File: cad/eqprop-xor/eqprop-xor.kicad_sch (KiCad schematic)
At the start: 31 parts, among them J1 USB_C_Receptacle_USB2.0_14P, U1 MCP6004, U2 LM324

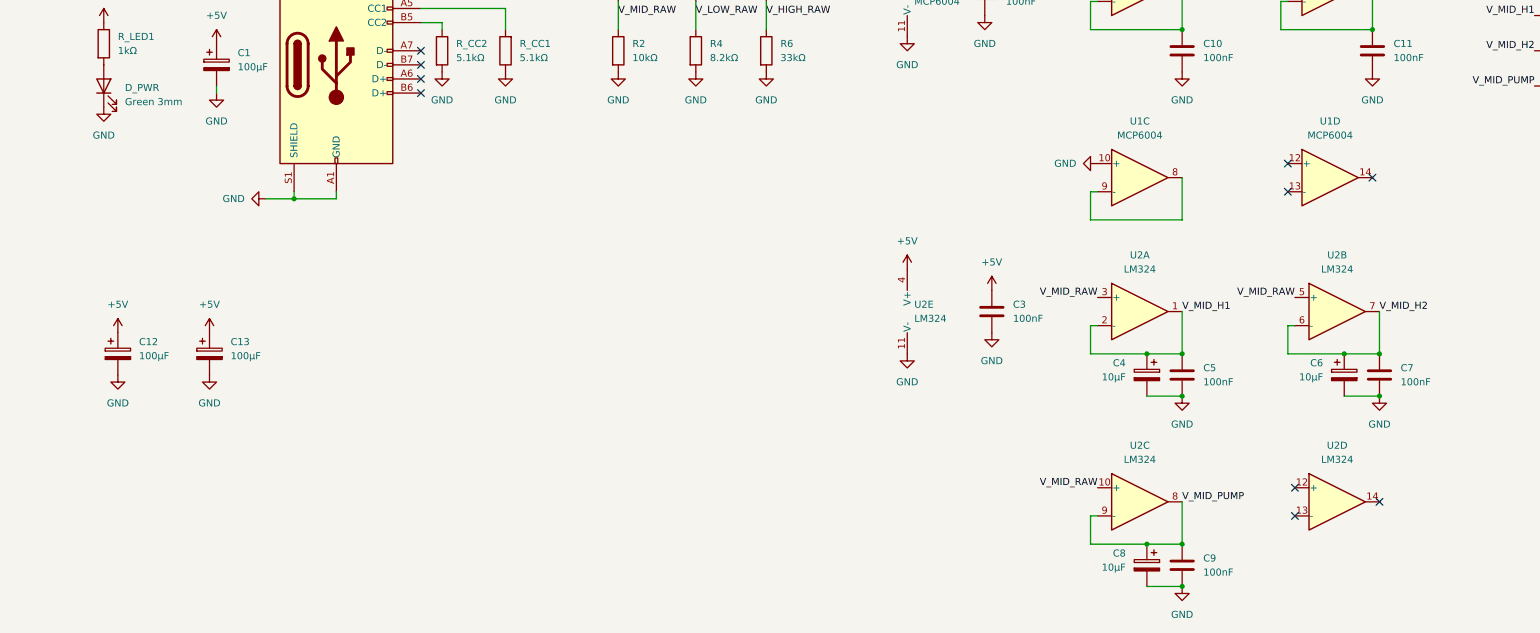
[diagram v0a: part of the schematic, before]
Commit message: Add Arduino Nano section with CS pull-ups and text annotations
Section 2: Arduino Nano pin assignments, 9x 10kΩ CS pull-up resistors,
bulk decoupling caps placed near analog/digital clusters, and text
annotations for readability.

Co-Authored-By: Claude Opus 4.6 <noreply@anthropic.com>
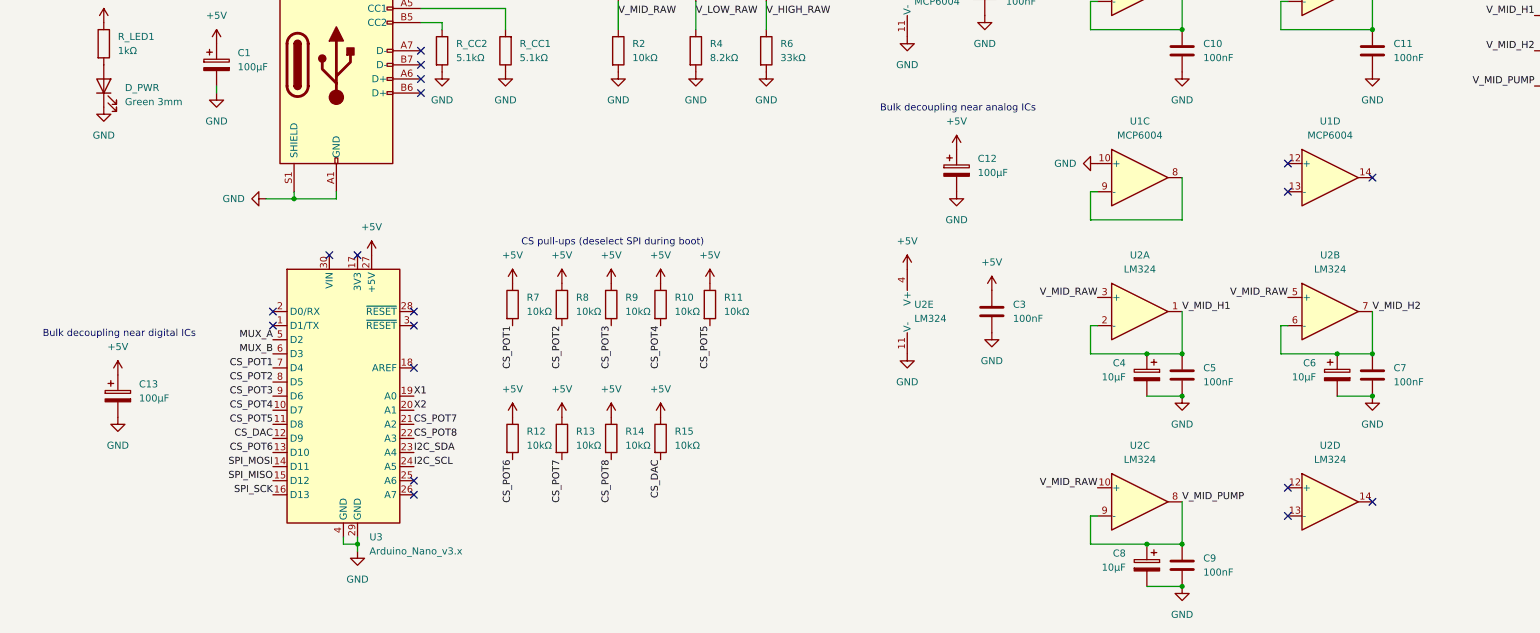
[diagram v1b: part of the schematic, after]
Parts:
- added R10, R11, R12, R13, R14, R15, R7, R8, R9: 10kΩ, symbol Device:R
- added U3: Arduino_Nano_v3.x, Module:Arduino_Nano, symbol MCU_Module:Arduino_Nano_v3.x
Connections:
- net +5V: now also R10.1, R11.1, R12.1, R13.1, R14.1, R15.1, R7.1, R8.1, R9.1, U3.27 (+5V)
- net GND: now also U3.29 (GND), U3.4 (GND)
- new net CS_DAC: R15.2, U3.12 (D9)
- new net CS_POT1: R7.2, U3.7 (D4)
- new net CS_POT2: R8.2, U3.8 (D5)
- new net CS_POT3: R9.2, U3.9 (D6)
- new net CS_POT4: R10.2, U3.10 (D7)
- new net CS_POT5: R11.2, U3.11 (D8)
- new net CS_POT6: R12.2, U3.13 (D10)
- new net CS_POT7: R13.2, U3.21 (A2)
- new net CS_POT8: R14.2, U3.22 (A3)
- new net I2C_SCL: U3.24 (A5)
- new net I2C_SDA: U3.23 (A4)
- new net MUX_A: U3.5 (D2)
- new net MUX_B: U3.6 (D3)
- new net SPI_MISO: U3.15 (D12)
- new net SPI_MOSI: U3.14 (D11)
- new net SPI_SCK: U3.16 (D13)
- new net X1: U3.19 (A0)
- new net X2: U3.20 (A1)
- no-connect marks 10 -> 19
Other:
- note added: "Bulk decoupling near analog ICs"
- note added: "Bulk decoupling near digital ICs"
- note added: "CS pull-ups (deselect SPI during boot)"
- moved on the sheet: C12, C13, C6, C7, U2B, U2D

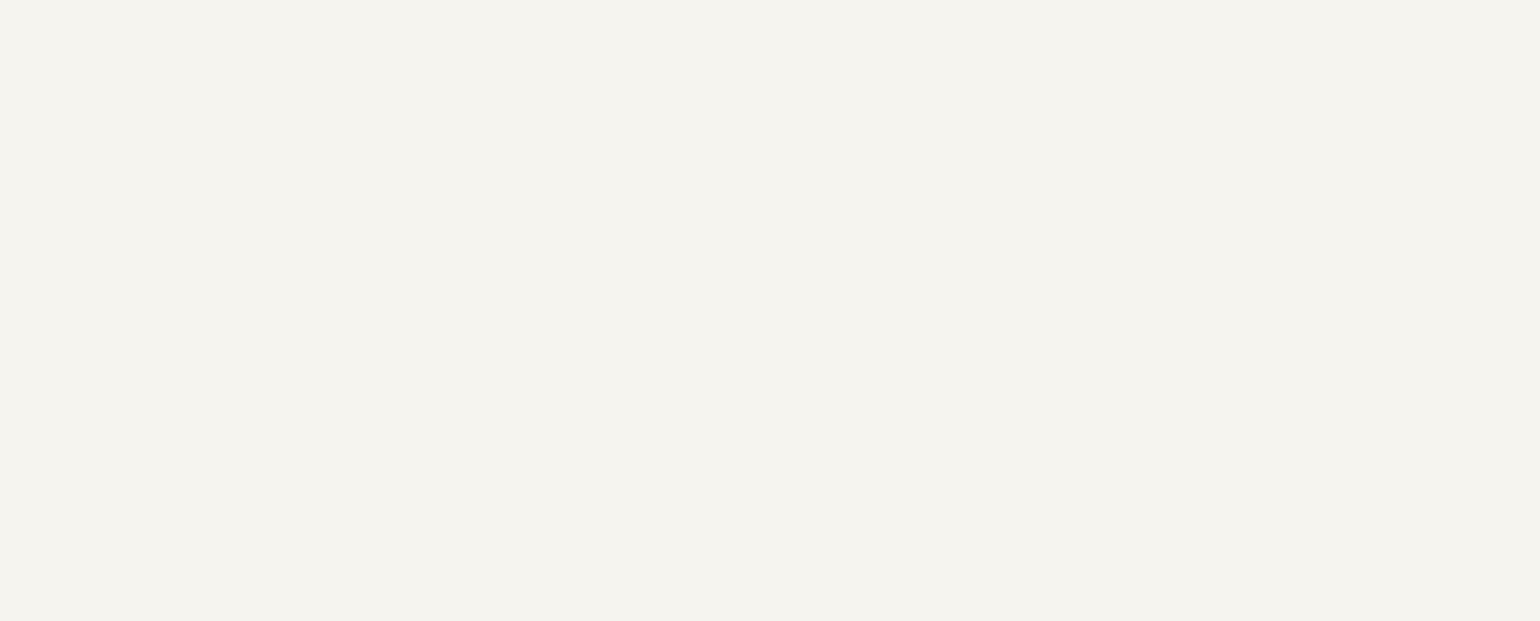
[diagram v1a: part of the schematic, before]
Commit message: Add input muxes and inference toggle switches
Section 3: 2x CD4053B analog muxes (direct + complementary inputs),
decoupling caps, SPDT toggle switches with 10kΩ isolation resistors
for inference mode.

Co-Authored-By: Claude Opus 4.6 <noreply@anthropic.com>
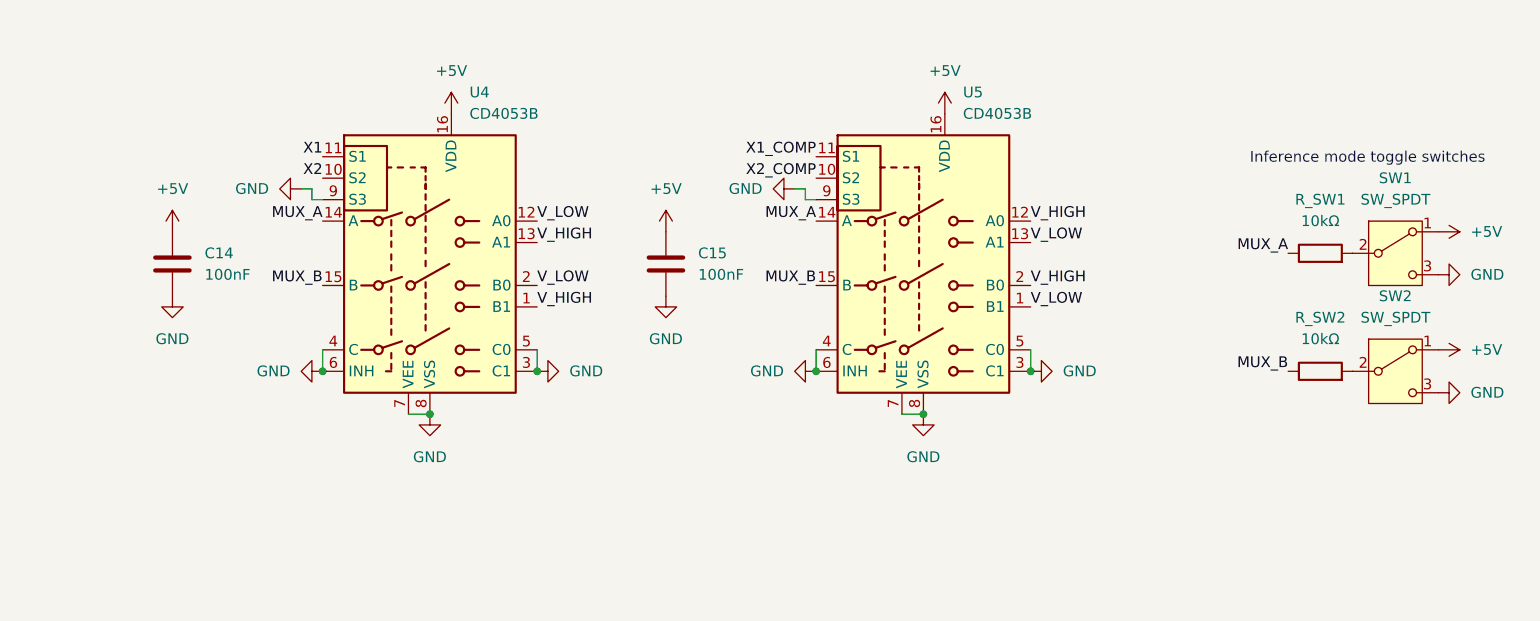
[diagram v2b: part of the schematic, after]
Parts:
- added C14, C15: 100nF, symbol Device:C
- added R_SW1, R_SW2: 10kΩ, symbol Device:R
- added SW1, SW2: SW_SPDT, symbol Switch:SW_SPDT
- added U4, U5: CD4053B, symbol Analog_Switch:CD4053B
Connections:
- net +5V: now also C14.1, C15.1, SW1.1 (A), SW2.1 (A), U4.16 (VDD), U5.16 (VDD)
- net GND: now also C14.2, C15.2, SW1.3 (C), SW2.3 (C), U4.3 (C1), U4.4 (C), U4.5 (C0), U4.6 (INH), U4.7 (VEE), U4.8 (VSS), U4.9 (S3), U5.3 (C1), U5.4 (C), U5.5 (C0), U5.6 (INH), U5.7 (VEE), U5.8 (VSS), U5.9 (S3)
- net MUX_A: now also R_SW1.1, U4.14 (A), U5.14 (A)
- net MUX_B: now also R_SW2.1, U4.15 (B), U5.15 (B)
- net V_HIGH: now also U4.1 (B1), U4.13 (A1), U5.12 (A0), U5.2 (B0)
- net V_LOW: now also U4.12 (A0), U4.2 (B0), U5.1 (B1), U5.13 (A1)
- net X1: now also U4.11 (S1)
- net X2: now also U4.10 (S2)
- new net: R_SW2.2, SW2.2 (B)
- new net: R_SW1.2, SW1.2 (B)
- new net X1_COMP: U5.11 (S1)
- new net X2_COMP: U5.10 (S2)
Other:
- note added: "Inference mode toggle switches"

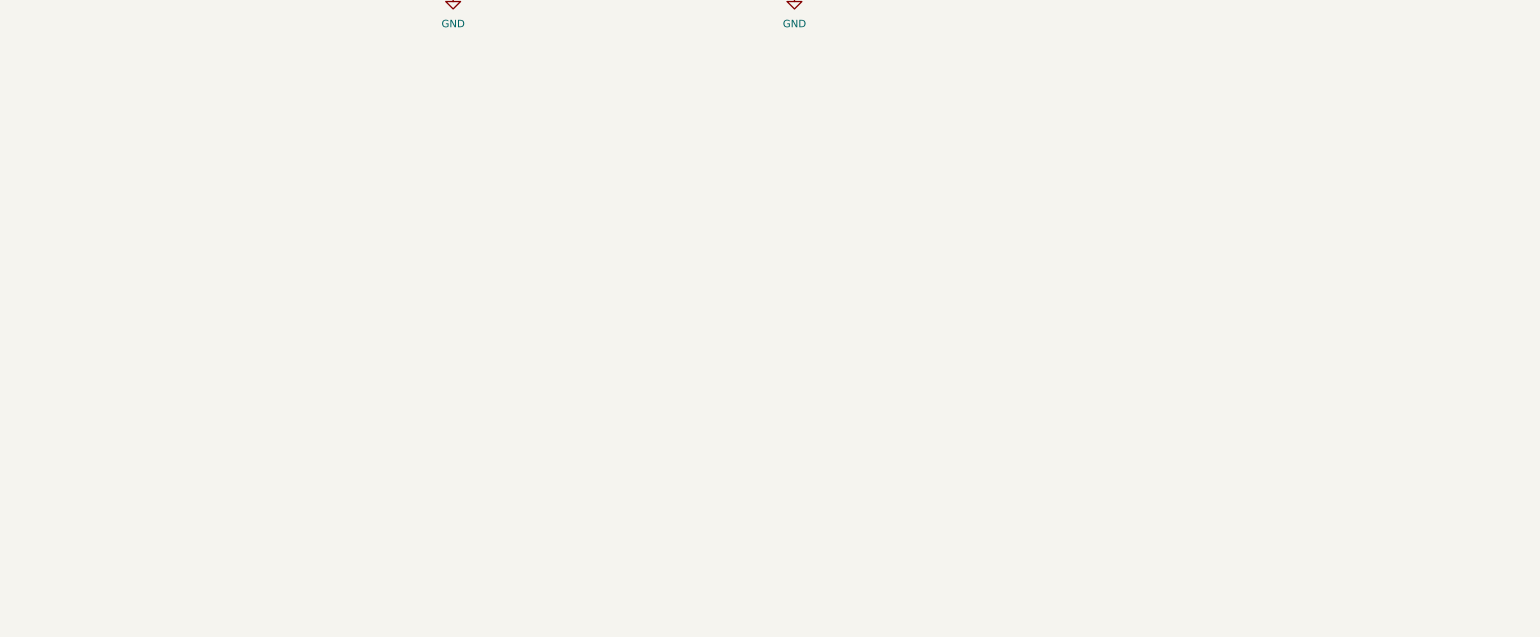
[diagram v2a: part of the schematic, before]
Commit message: Add 8x MCP4251 weight resistors with series protection
Section 4: 8x MCP4251-104 digital potentiometers (16 weight channels),
16x 1.21kΩ series protection resistors, and 8x 100nF decoupling caps.

Co-Authored-By: Claude Opus 4.6 <noreply@anthropic.com>
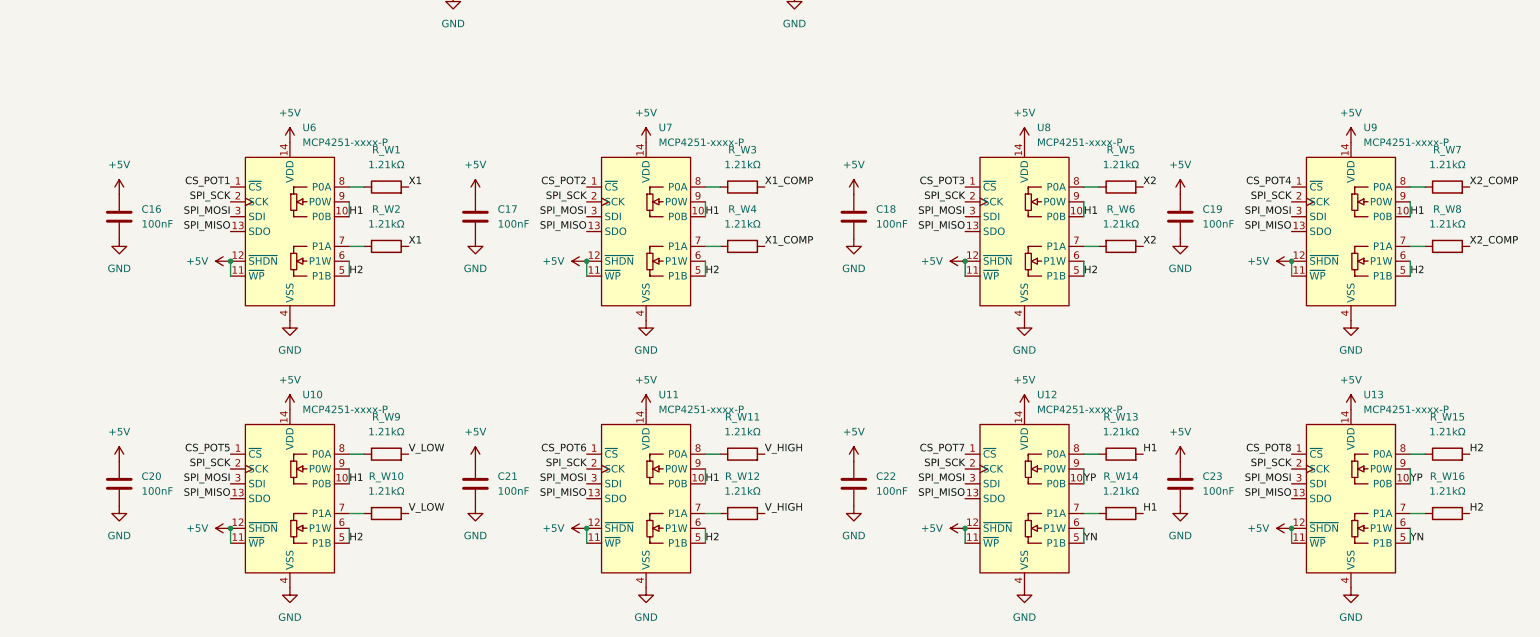
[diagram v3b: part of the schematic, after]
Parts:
- added C16, C17, C18, C19, C20, C21, C22, C23: 100nF, symbol Device:C
- added R_W1, R_W10, R_W11, R_W12, R_W13, R_W14, R_W15, R_W16, R_W2, R_W3, R_W4, R_W5, R_W6, R_W7, R_W8, R_W9: 1.21kΩ, symbol Device:R
- added U10, U11, U12, U13, U6, U7, U8, U9: MCP4251-xxxx-P, Package_DIP:DIP-14_W7.62mm, symbol Potentiometer_Digital:MCP4251-xxxx-P
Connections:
- net +5V: now also C16.1, C17.1, C18.1, C19.1, C20.1, C21.1, C22.1, C23.1, U10.11 (~{WP}), U10.12 (~{SHDN}), U10.14 (VDD), U11.11 (~{WP}), U11.12 (~{SHDN}), U11.14 (VDD), U12.11 (~{WP}), U12.12 (~{SHDN}), U12.14 (VDD), U13.11 (~{WP}), U13.12 (~{SHDN}), U13.14 (VDD), U6.11 (~{WP}), U6.12 (~{SHDN}), U6.14 (VDD), U7.11 (~{WP}), U7.12 (~{SHDN}), U7.14 (VDD), U8.11 (~{WP}), U8.12 (~{SHDN}), U8.14 (VDD), U9.11 (~{WP}), U9.12 (~{SHDN}), U9.14 (VDD)
- net CS_POT1: now also U6.1 (~{CS})
- net CS_POT2: now also U7.1 (~{CS})
- net CS_POT3: now also U8.1 (~{CS})
- net CS_POT4: now also U9.1 (~{CS})
- net CS_POT5: now also U10.1 (~{CS})
- net CS_POT6: now also U11.1 (~{CS})
- net CS_POT7: now also U12.1 (~{CS})
- net CS_POT8: now also U13.1 (~{CS})
- net GND: now also C16.2, C17.2, C18.2, C19.2, C20.2, C21.2, C22.2, C23.2, U10.4 (VSS), U11.4 (VSS), U12.4 (VSS), U13.4 (VSS), U6.4 (VSS), U7.4 (VSS), U8.4 (VSS), U9.4 (VSS)
- net SPI_MISO: now also U10.13 (SDO), U11.13 (SDO), U12.13 (SDO), U13.13 (SDO), U6.13 (SDO), U7.13 (SDO), U8.13 (SDO), U9.13 (SDO)
- net SPI_MOSI: now also U10.3 (SDI), U11.3 (SDI), U12.3 (SDI), U13.3 (SDI), U6.3 (SDI), U7.3 (SDI), U8.3 (SDI), U9.3 (SDI)
- net SPI_SCK: now also U10.2 (SCK), U11.2 (SCK), U12.2 (SCK), U13.2 (SCK), U6.2 (SCK), U7.2 (SCK), U8.2 (SCK), U9.2 (SCK)
- net V_HIGH: now also R_W11.2, R_W12.1
- net V_LOW: now also R_W10.1, R_W9.2
- net X1: now also R_W1.2, R_W2.1
- net X1_COMP: now also R_W3.2, R_W4.1
- net X2: now also R_W5.2, R_W6.1
- net X2_COMP: now also R_W7.2, R_W8.1
- new net: R_W10.2, U10.7 (P1A)
- new net: R_W9.1, U10.8 (P0A)
- new net: R_W11.1, U11.8 (P0A)
- new net: R_W12.2, U11.7 (P1A)
- new net: R_W14.2, U12.7 (P1A)
- new net: R_W4.2, U7.7 (P1A)
- new net: R_W13.1, U12.8 (P0A)
- new net: R_W3.1, U7.8 (P0A)
- new net: R_W8.2, U9.7 (P1A)
- new net: R_W6.2, U8.7 (P1A)
- new net: R_W16.2, U13.7 (P1A)
- new net: R_W7.1, U9.8 (P0A)
- new net: R_W1.1, U6.8 (P0A)
- new net: R_W2.2, U6.7 (P1A)
- new net: R_W15.1, U13.8 (P0A)
- new net: R_W5.1, U8.8 (P0A)
- new net H1: R_W13.2, R_W14.1, U10.10 (P0B), U10.9 (P0W), U11.10 (P0B), U11.9 (P0W), U6.10 (P0B), U6.9 (P0W), U7.10 (P0B), U7.9 (P0W), U8.10 (P0B), U8.9 (P0W), U9.10 (P0B), U9.9 (P0W)
- new net H2: R_W15.2, R_W16.1, U10.5 (P1B), U10.6 (P1W), U11.5 (P1B), U11.6 (P1W), U6.5 (P1B), U6.6 (P1W), U7.5 (P1B), U7.6 (P1W), U8.5 (P1B), U8.6 (P1W), U9.5 (P1B), U9.6 (P1W)
- new net YN: U12.5 (P1B), U12.6 (P1W), U13.5 (P1B), U13.6 (P1W)
- new net YP: U12.10 (P0B), U12.9 (P0W), U13.10 (P0B), U13.9 (P0W)

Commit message: Add section labels and title block annotations
Co-Authored-By: Claude Opus 4.6 <noreply@anthropic.com>
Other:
- note added: "INPUT MULTIPLEXERS"
- note added: "MICROCONTROLLER"
- note added: "POWER + VOLTAGE REFERENCES"
- note added: "WEIGHT NETWORK"
- moved on the sheet: C13, R1, R10, R11, R12, R13, R14, R15, R2, R3, R4, R5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

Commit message: Complete schematic: sections 5-7 and documentation update
Sections 5-7: BAT42 activation diodes with solder bridge pads,
MCP4822 DAC + MCP6002 Howland current pumps, ADS1115 ADC with
I2C pull-ups, and LED comparators on U1D/U2D.

Updated KiCad overview doc to be a concise reference with KiCad 9
notes (symbol naming, CD4053B pin mapping, footprint assignment).

Co-Authored-By: Claude Opus 4.6 <noreply@anthropic.com>
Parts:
- added C24, C25, C26: 100nF, symbol Device:C
- added D1, D2, D3, D4: BAT42, Diode_THT:D_DO-35_SOD27_P7.62mm_Horizontal, symbol Diode:BAT42
- added D5, D_GRN: LED, symbol Device:LED
- added R16, R17, R18, R19: 0Ω, symbol Device:R
- added R20, R21: 4.7kΩ, symbol Device:R
- added R_H1, R_H2, R_H3, R_H4, R_H5, R_H6, R_H7, R_H8: 10kΩ, symbol Device:R
- added R_LED_G, R_LED_R: 470Ω, symbol Device:R
- added R_SET_A, R_SET_B: 1MΩ, symbol Device:R
- added TP10, TP11, TP6, TP7, TP8, TP9: TestPoint, symbol Connector:TestPoint
- added U14: MCP4822, symbol Analog_DAC:MCP4822
- added U15: MCP6002-xP, symbol Amplifier_Operational:MCP6002-xP
- added U16: ADS1115IDGS, Package_SO:TSSOP-10_3x3mm_P0.5mm, symbol Analog_ADC:ADS1115IDGS
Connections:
- net +5V: now also C24.1, C25.1, R20.1, R21.1, R_LED_G.2, R_LED_R.2, U14.1 (Vdd), U15.8 (V+), U16.8 (VDD)
- net CS_DAC: now also U14.2 (~{CS})
- net GND: now also C24.2, C25.2, U14.5 (~{LDAC}), U14.7 (Vss), U15.4 (V-), U16.1 (ADDR), U16.3 (GND)
- net H1: now also D1.2 (A), R17.1, TP6.1, U16.4 (AIN0)
- net H2: now also D3.2 (A), R18.1, TP7.1, U16.5 (AIN1)
- net I2C_SCL: now also R21.2, U16.10 (SCL)
- net I2C_SDA: now also R20.2, U16.9 (SDA)
- net SPI_MOSI: now also U14.4 (SDI)
- net SPI_SCK: now also U14.3 (SCK)
- net V_MID_H1: now also D2.2 (A), R16.2
- net V_MID_H2: now also D4.2 (A), R19.2
- net V_MID_PUMP: now also R_H2.1, R_H6.1
- net YN: now also U1.12 (+), U2.13 (-), R_H8.2, R_SET_B.1, TP11.1, U16.7 (AIN3)
- net YP: now also U1.13 (-), U2.12 (+), R_H4.2, R_SET_A.2, TP10.1, U16.6 (AIN2)
- net at U1.14: now also D_GRN.1 (K)
- net at U2.14: now also D5.1 (K)
- new net: D4.1 (K), R18.2
- new net: R_H1.2, R_SET_A.1, U15.3 (+)
- new net: D1.1 (K), R16.1
- new net: R_H3.1, R_H4.1, U15.1
- new net: R_H2.2, R_H3.2, U15.2 (-)
- new net: D3.1 (K), R19.1
- new net: R_H5.2, R_SET_B.2, U15.5 (+)
- new net: R_H6.2, R_H7.2, U15.6 (-)
- new net: D_GRN.2 (A), R_LED_G.1
- new net: D5.2 (A), R_LED_R.1
- new net: D2.1 (K), R17.2
- new net: R_H7.1, R_H8.1, U15.7
- new net DAC_OUTA: R_H1.1, TP8.1, U14.8 (VA)
- new net DAC_OUTB: R_H5.1, TP9.1, U14.6 (VB)
- no-connect marks 19 -> 14
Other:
- note added: "NUDGE CURRENT INJECTION"
- moved on the sheet: C16, C17, C18, C19, C20, C21, C22, C23, R_W1, R_W10, R_W11, R_W12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
